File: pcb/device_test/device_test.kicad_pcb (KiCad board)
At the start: 2 copper layers, 170 x 55 mm, 0 parts

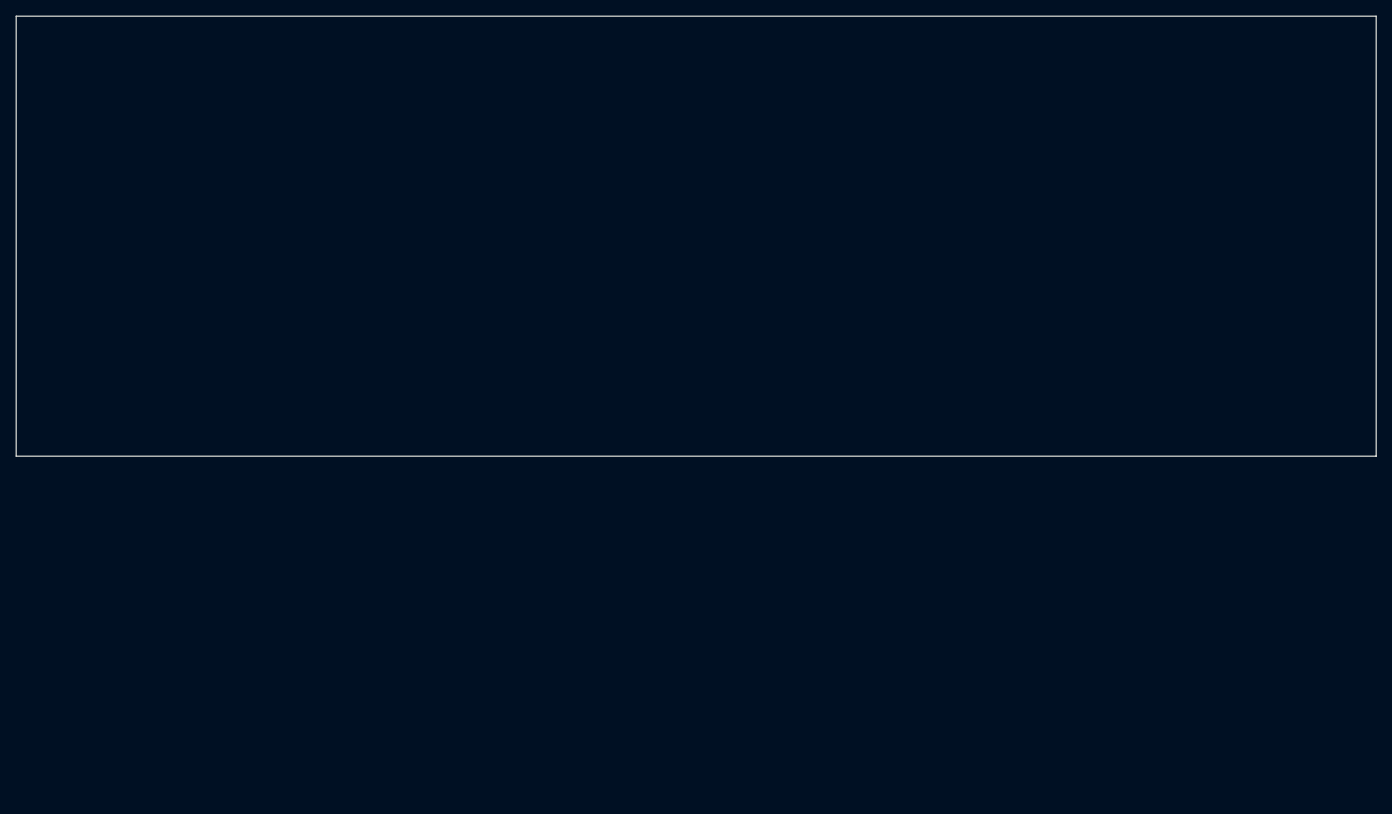
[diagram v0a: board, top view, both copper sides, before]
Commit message: update pcb limits and add other pcb setup
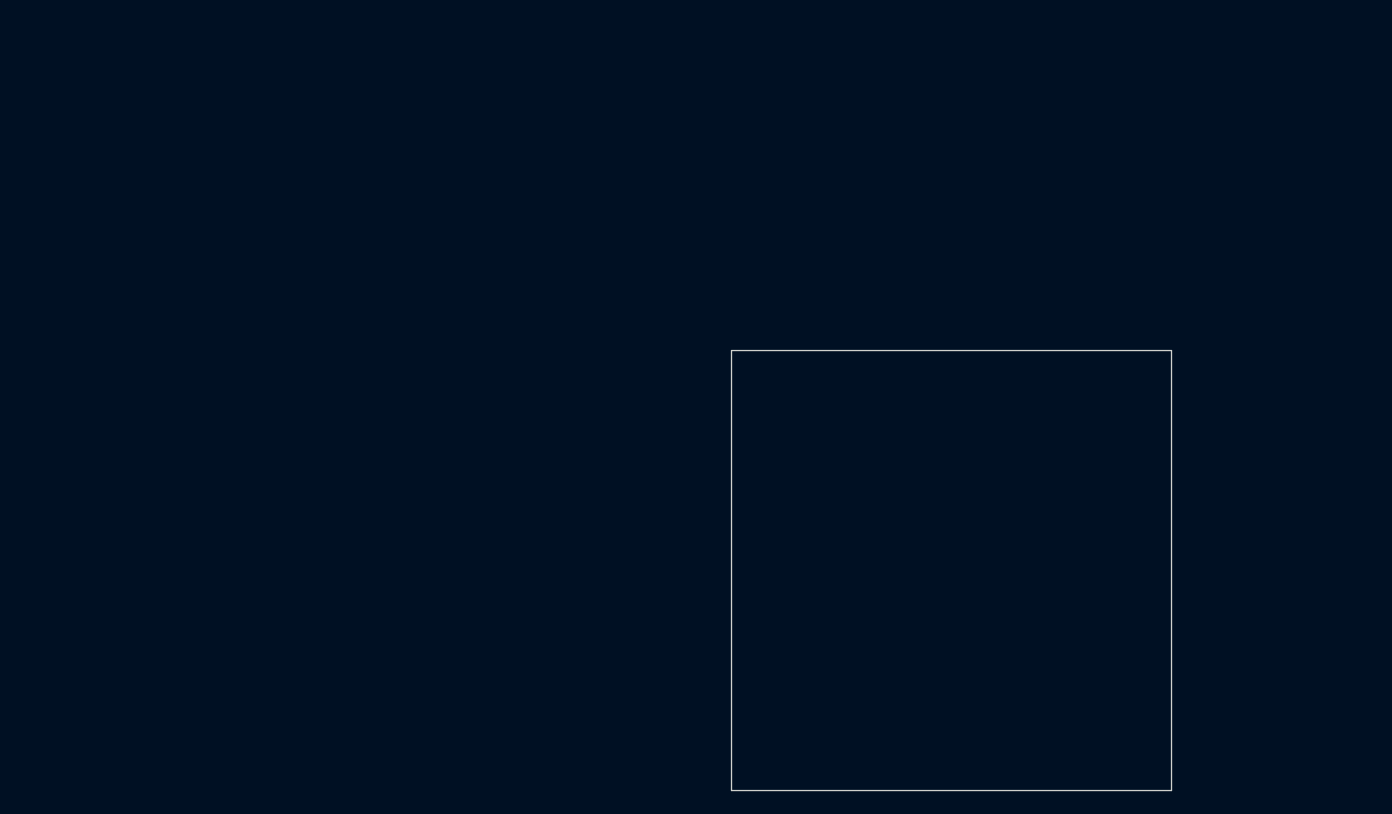
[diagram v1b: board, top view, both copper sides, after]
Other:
- board size 170 x 55 mm -> 55 x 55 mm
- copper layers 2 -> 4
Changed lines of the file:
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@@
 	(generator_version "8.0")
 	(general
-		(thickness 1.6)
+		(thickness 1.6062)
 		(legacy_teardrops no)
 	)
@@
 	(layers
 		(0 "F.Cu" signal)
+		(1 "In1.Cu" power)
+		(2 "In2.Cu" power)
 		(31 "B.Cu" signal)
 		(32 "B.Adhes" user "B.Adhesive")
@@
 	)
 	(setup
+		(stackup
+			(layer "F.SilkS"
+				(type "Top Silk Screen")
+				(color "White")
+			)
+			(layer "F.Paste"
+				(type "Top Solder Paste")
+			)
+			(layer "F.Mask"
+				(type "Top Solder Mask")
+				(color "Green")
+				(thickness 0.01)
+			)
+			(layer "F.Cu"
+				(type "copper")
+				(thickness 0.035)
+			)
+			(layer "dielectric 1"
+				(type "prepreg")
+				(color "FR4 natural")
+				(thickness 0.2104)
+				(material "FR4")
+				(epsilon_r 4.4)
+				(loss_tangent 0.02)
+			)
+			(layer "In1.Cu"
+				(type "copper")
+				(thickness 0.0152)
+			)
+			(layer "dielectric 2"
+				(type "core")
+				(color "FR4 natural")
+				(thickness 1.065)
+				(material "FR4")
+				(epsilon_r 4.6)
+				(loss_tangent 0.02)
+			)
+			(layer "In2.Cu"
+				(type "copper")
+				(thickness 0.0152)
+			)
+			(layer "dielectric 3"
+				(type "prepreg")
+				(color "FR4 natural")
+				(thickness 0.2104)
+				(material "FR4")
+				(epsilon_r 4.4)
+				(loss_tangent 0.02)
+			)
+			(layer "B.Cu"
+				(type "copper")
+				(thickness 0.035)
+			)
+			(layer "B.Mask"
+				(type "Bottom Solder Mask")
+				(color "Green")
+				(thickness 0.01)
+			)
+			(layer "B.Paste"
+				(type "Bottom Solder Paste")
+			)
+			(layer "B.SilkS"
+				(type "Bottom Silk Screen")
+				(color "White")
+			)
+			(copper_finish "ENIG")
+			(dielectric_constraints yes)
+		)
 		(pad_to_mask_clearance 0)
 		(allow_soldermask_bridges_in_footprints no)
@@
 	(net 0 "")
 	(gr_rect
-		(start 26.342 21.454)
-		(end 196.342 76.454)
+		(start 115.756 63.246)
+		(end 170.756 118.246)
 		(stroke
 			(width 0.05)

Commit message: pcb update
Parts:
- added D101: LED, LED_SMD:LED_0805_2012Metric, F.Cu at (158.4, 83.6)
- added D102: LED, LED_SMD:LED_0805_2012Metric, F.Cu at (152.3, 77.2)
- added D103: LED, LED_SMD:LED_0805_2012Metric, F.Cu at (124.4, 97.3)
- added J101: Screw_Terminal_01x02, TerminalBlock_Phoenix:TerminalBlock_Phoenix_MKDS-1,5-2_1x02_P5.00mm_Horizontal, F.Cu at (166.9, 87.6)
- added J102: Conn_01x05, Connector_PinSocket_2.54mm:PinSocket_1x05_P2.54mm_Horizontal, F.Cu at (136.1, 73.2)
- added J103: Conn_01x05, Connector_PinHeader_2.54mm:PinHeader_1x05_P2.54mm_Horizontal, F.Cu at (119.8, 83.6)
- added J104: USB_OTG, USB:MicroUSB-920-E52A2021S10100, F.Cu at (147.0, 116.0)
- added J105: USB_A, USB:USB_A_C456020, F.Cu at (160.0, 103.4)
- added J106: Conn_01x07, Connector_PinSocket_2.54mm:PinSocket_1x07_P2.54mm_Horizontal, F.Cu at (164.0, 73.1)
- added J107: Conn_01x06, Connector_PinHeader_2.54mm:PinHeader_1x06_P2.54mm_Horizontal, F.Cu at (119.8, 109.0)
- added R101: 1k8, Resistor_SMD:R_0805_2012Metric, F.Cu at (158.4, 87.4)
- added R102: 360, Resistor_SMD:R_0805_2012Metric, F.Cu at (152.3, 79.8)
- added R103: 360, Resistor_SMD:R_0805_2012Metric, F.Cu at (127.2, 97.3)
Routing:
- net +12V: track 0.00 -> 53.6 mm
- net /USB1+: track 0.00 -> 48.1 mm, vias 0 -> 1
- net /USB1-: track 0.00 -> 47.5 mm, vias 0 -> 1
- net +5V_A: track 0.00 -> 46.0 mm, vias 0 -> 2
- net /USB_OTG_ID: track 0.00 -> 44.8 mm, vias 0 -> 1
- net /USB2-: track 0.00 -> 43.4 mm
- net +5V_B: track 0.00 -> 43.1 mm
- net /USB2+: track 0.00 -> 40.8 mm, vias 0 -> 2
- net GND: track 0.00 -> 5.03 mm, vias 0 -> 3
- net Net-(D103-K): track 0.00 -> 2.80 mm
- net Net-(D102-K): track 0.00 -> 2.55 mm
- net Net-(D101-K): track 0.00 -> 1.96 mm
- added copper zone on In1.Cu, net GND
- added copper zone on In2.Cu, net GND
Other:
- board size 55 x 55 mm -> 55.9 x 55.9 mm
- board text added: "12V"
- board text added: "5.080mm"
- board text added: "5V"
- board text added: "7.620mm"
- board text added: "<HASH>"
- board text added: "Copyright by Amateurfunkclub für Remote Stationen"
- board text added: "Device Tester"

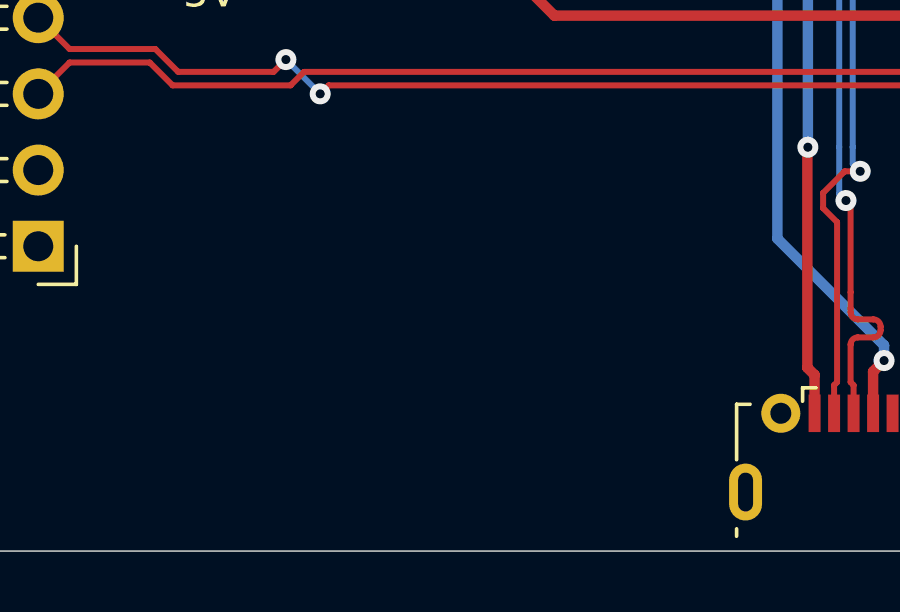
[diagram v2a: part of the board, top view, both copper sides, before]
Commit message: add logo
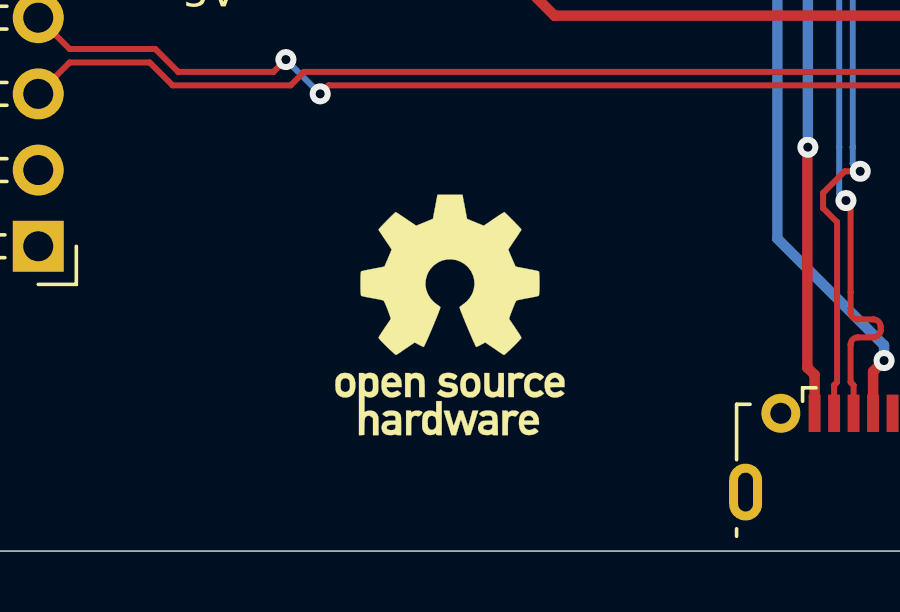
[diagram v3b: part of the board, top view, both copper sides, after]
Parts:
- added REF**: OSHW-Logo_7.5x8mm_SilkScreen, Symbol:OSHW-Logo_7.5x8mm_SilkScreen, F.Cu at (133.5, 111.3)

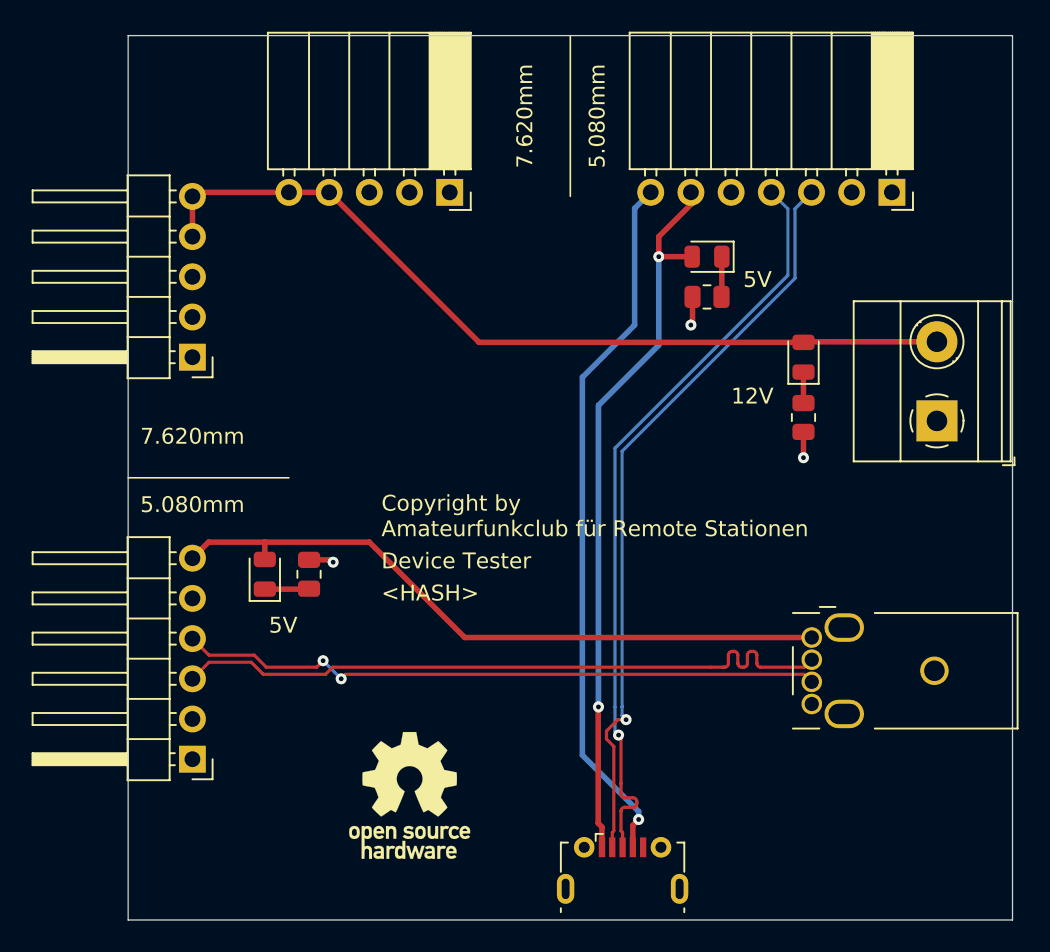
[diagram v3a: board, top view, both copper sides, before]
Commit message: update connectors
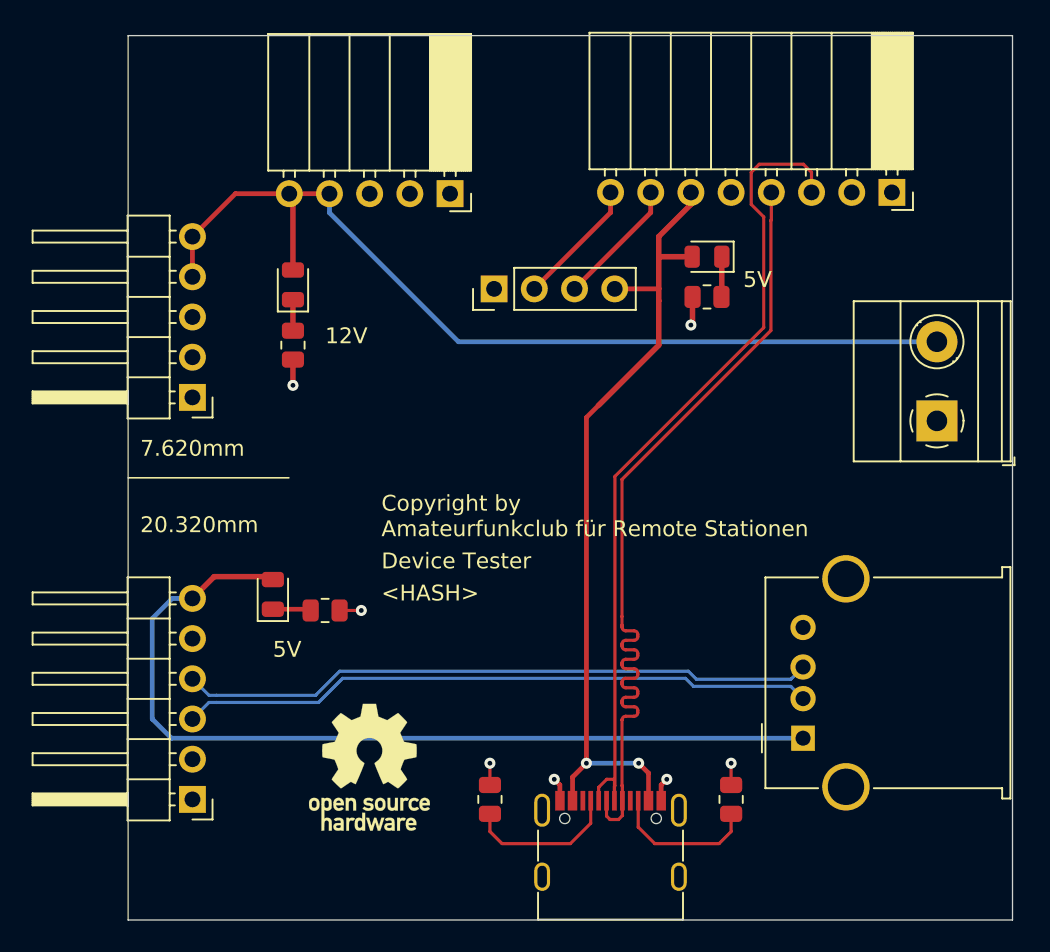
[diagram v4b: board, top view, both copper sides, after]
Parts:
- removed D102, D103: LED, LED_SMD:LED_0805_2012Metric
- removed J102: Conn_01x05, Connector_PinSocket_2.54mm:PinSocket_1x05_P2.54mm_Horizontal
- removed J103: Conn_01x05, Connector_PinHeader_2.54mm:PinHeader_1x05_P2.54mm_Horizontal
- removed J104: USB_OTG, USB:MicroUSB-920-E52A2021S10100
- removed J105: USB_A, USB:USB_A_C456020
- removed J106: Conn_01x07, Connector_PinSocket_2.54mm:PinSocket_1x07_P2.54mm_Horizontal
- removed J107: Conn_01x06, Connector_PinHeader_2.54mm:PinHeader_1x06_P2.54mm_Horizontal
- removed R102, R103: 360, Resistor_SMD:R_0805_2012Metric
- removed REF**: OSHW-Logo_7.5x8mm_SilkScreen, Symbol:OSHW-Logo_7.5x8mm_SilkScreen
- added #SYM101: OSHW-Logo_7.5x8mm_SilkScreen, Symbol:OSHW-Logo_7.5x8mm_SilkScreen, F.Cu at (131.0, 109.5)
- added #SYM101: OSHW-Logo_7.5x8mm_SilkScreen, Symbol:OSHW-Logo_7.5x8mm_SilkScreen, B.Cu at (131.0, 109.5)
- added D201: LED, LED_SMD:LED_0805_2012Metric, F.Cu at (152.3, 77.2)
- added D301: LED, LED_SMD:LED_0805_2012Metric, F.Cu at (124.9, 98.6)
- added J201: Conn_01x05, Connector_PinSocket_2.54mm:PinSocket_1x05_P2.54mm_Horizontal, F.Cu at (136.1, 73.2)
- added J202: USB_C_Receptacle_USB2.0_16P, Connector_USB:USB_C_Receptacle_G-Switch_GT-USB-7010ASV, F.Cu at (146.2, 115.3)
- added J203: Conn_01x04, Connector_PinHeader_2.54mm:PinHeader_1x04_P2.54mm_Vertical, F.Cu at (138.9, 79.2)
- added J204: Conn_01x08, Connector_PinSocket_2.54mm:PinSocket_1x08_P2.54mm_Horizontal, F.Cu at (164.0, 73.2)
- added J301: Conn_01x05, Connector_PinHeader_2.54mm:PinHeader_1x05_P2.54mm_Horizontal, F.Cu at (119.8, 86.1)
- added J302: USB_A, Connector_USB:USB_A_Molex_67643_Horizontal, F.Cu at (158.4, 107.6)
- added J303: Conn_01x06, Connector_PinHeader_2.54mm:PinHeader_1x06_P2.54mm_Horizontal, F.Cu at (119.8, 111.5)
- added R201: 5k1, Resistor_SMD:R_0805_2012Metric, F.Cu at (138.6, 111.5)
- added R202: 5k1, Resistor_SMD:R_0805_2012Metric, F.Cu at (153.9, 111.5)
- added R203: 360, Resistor_SMD:R_0805_2012Metric, F.Cu at (152.3, 79.8)
- added R301: 360, Resistor_SMD:R_0805_2012Metric, F.Cu at (128.2, 99.6)
- moved D101 32.6 mm to (126.2, 79.0)
- moved R101 32.6 mm to (126.2, 82.8)
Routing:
- net /Device Tester Connector/USB+: track 0.00 -> 53.2 mm
- net /Device Tester Connector/USB-: track 0.00 -> 52.9 mm
- net /USB1+: track 48.1 -> 0.00 mm, vias 1 -> 0
- net /USB1-: track 47.5 -> 0.00 mm, vias 1 -> 0
- net /USB_OTG_ID: track 44.8 -> 0.00 mm, vias 1 -> 0
- net /USB2-: track 43.4 -> 0.00 mm
- net /USB2+: track 40.8 -> 0.00 mm, vias 2 -> 0
- net /Bus Tester Connector/USB-: track 0.00 -> 40.2 mm
- net /Bus Tester Connector/USB+: track 0.00 -> 40.2 mm
- net +5V_B: track 43.1 -> 56.4 mm
- net /Device Tester Connector/CC1: track 0.00 -> 9.76 mm
- net /Device Tester Connector/CC2: track 0.00 -> 9.40 mm
- net /Device Tester Connector/USB_OTG_ID: track 0.00 -> 8.45 mm
- net /Device Tester Connector/nRPIBOOT: track 0.00 -> 8.09 mm
- net +12V: track 53.6 -> 60.3 mm
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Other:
- board text added: "20.320mm"
- board text removed: "5.080mm"
